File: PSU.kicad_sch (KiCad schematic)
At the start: 11 parts, among them J1 Mini USB Female, J2 Battery Connector, U3 AMS1117-3.3

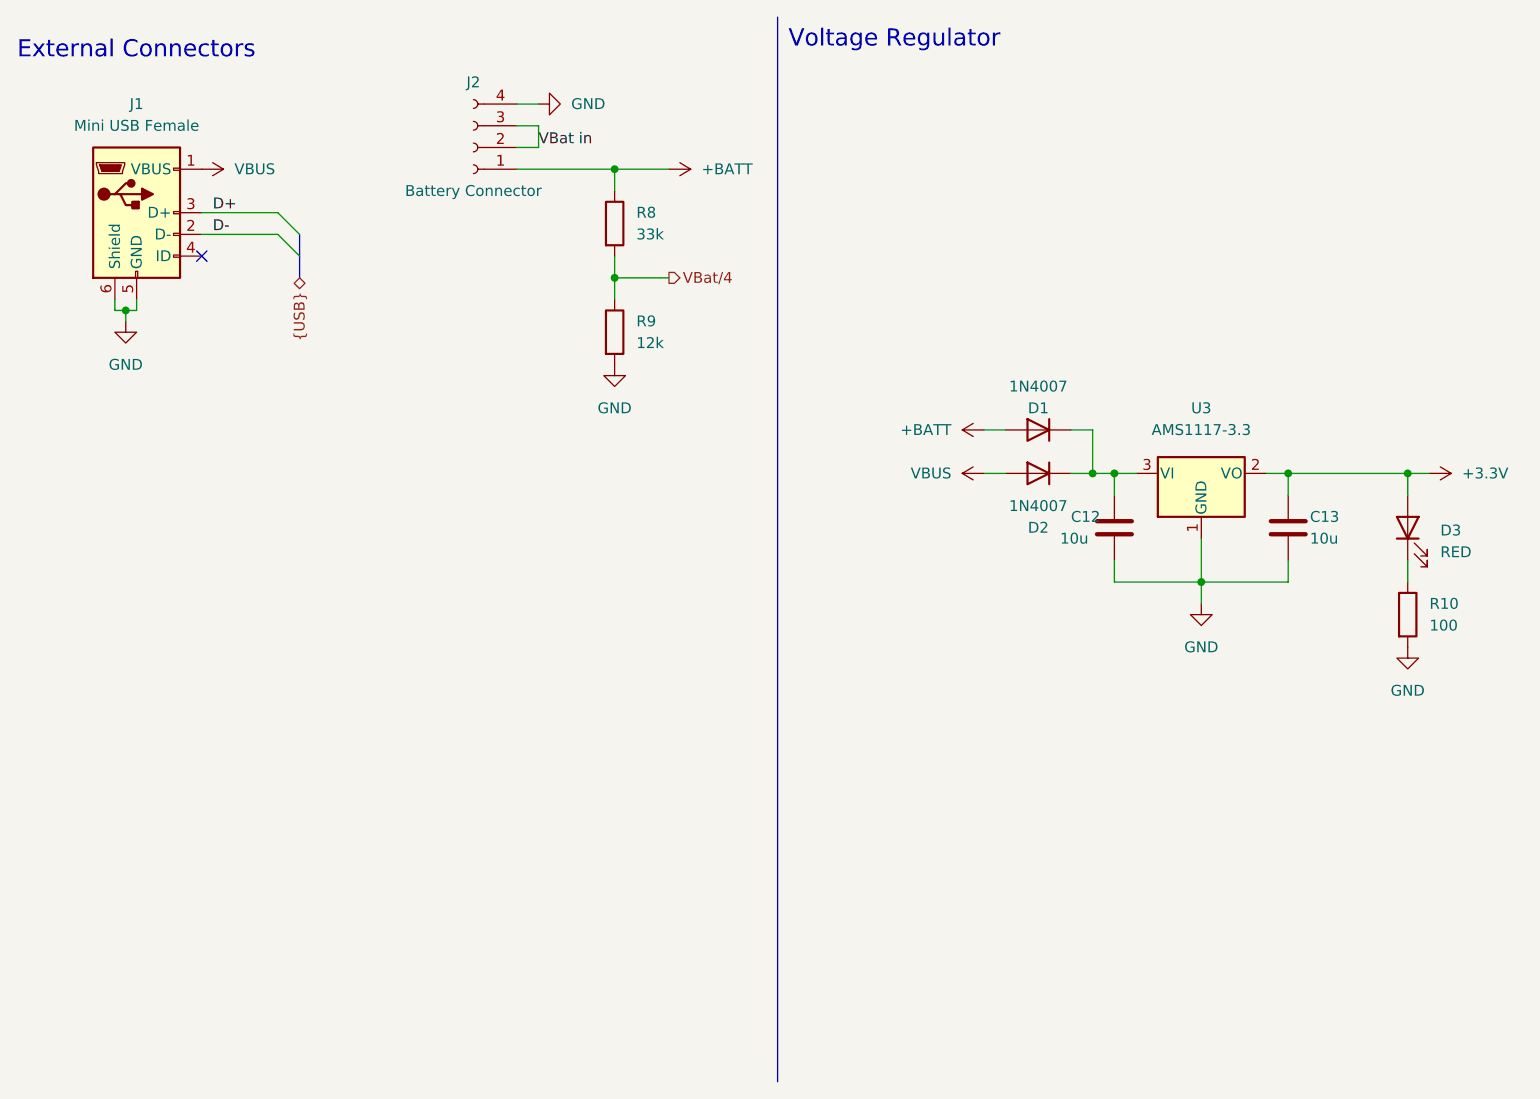
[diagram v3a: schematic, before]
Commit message: Connected the sensors, flash chip, Need to connect the radio and GPS
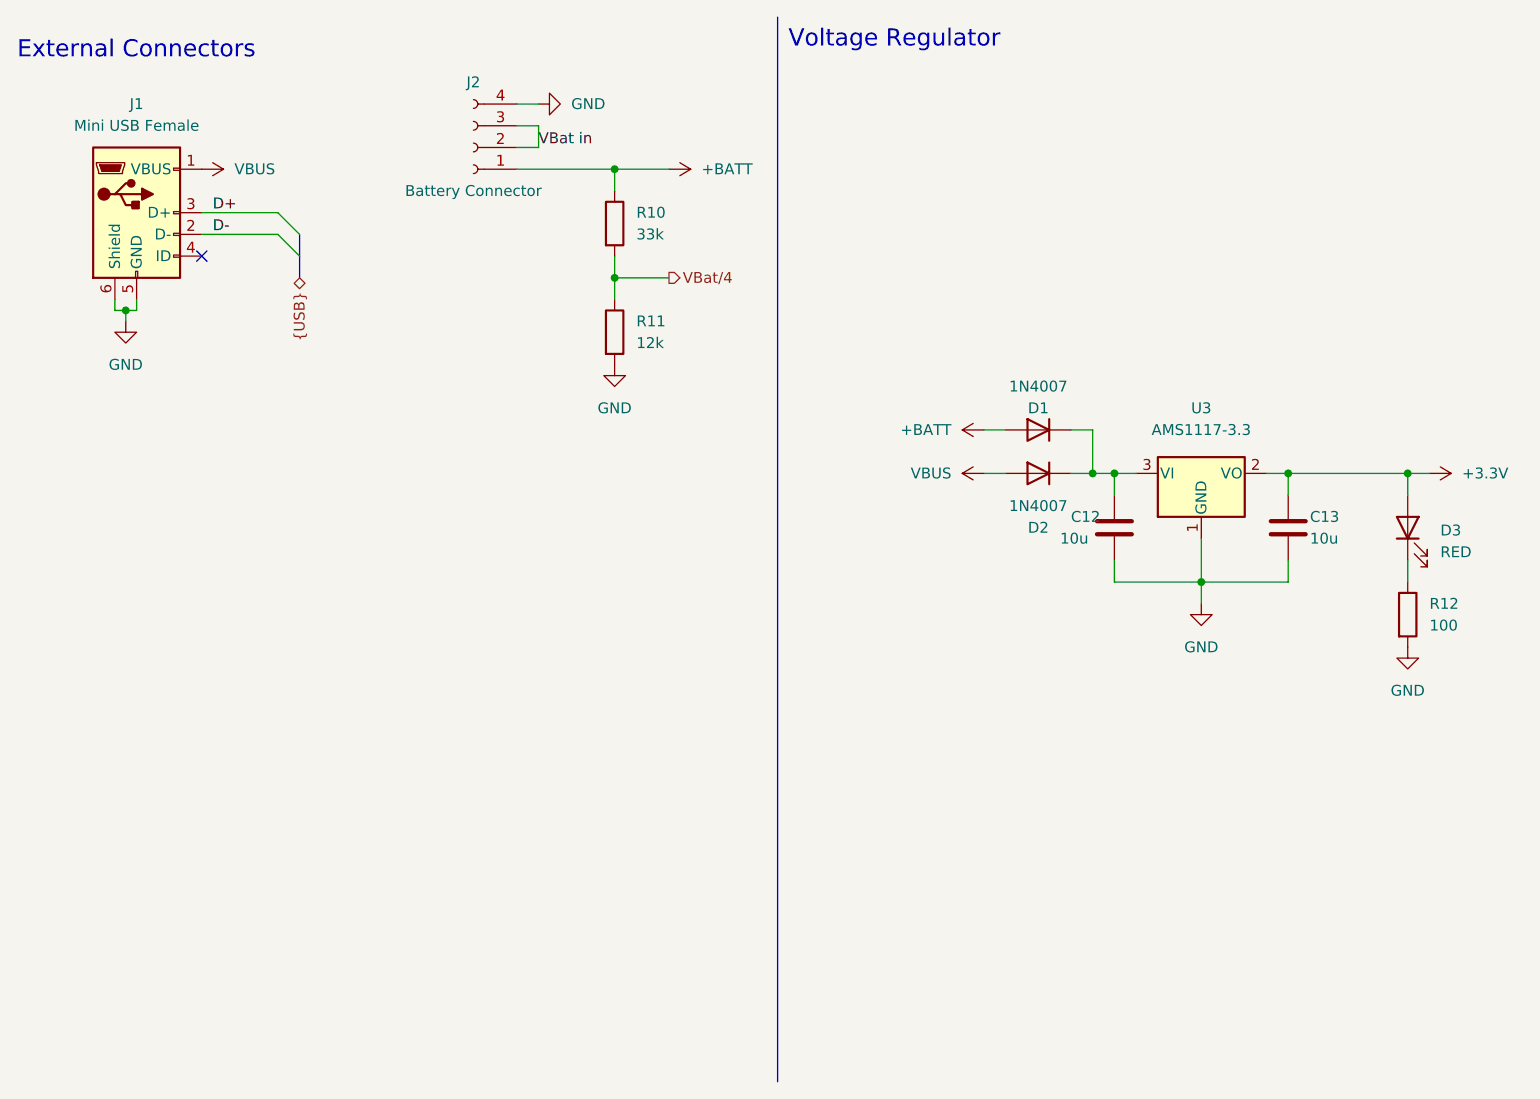
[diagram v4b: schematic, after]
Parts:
- renumbered R8 to R10, R9 to R11, R10 to R12
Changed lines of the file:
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@@
   (symbol (lib_id "power:+3.3V") (at 177.8 64.77 270) (unit 1)
     (in_bom yes) (on_board yes) (fields_autoplaced)
-    (property "Reference" "#PWR026" (id 0) (at 173.99 64.77 0)
+    (property "Reference" "#PWR027" (id 0) (at 173.99 64.77 0)
       (effects (font (size 1.27 1.27)) hide)
     )
@@
   (symbol (lib_id "Device:R") (at 82.55 35.56 0) (unit 1)
     (in_bom yes) (on_board yes) (fields_autoplaced)
-    (property "Reference" "R8" (id 0) (at 85.09 34.2899 0)
+    (property "Reference" "R10" (id 0) (at 85.09 34.2899 0)
       (effects (font (size 1.27 1.27)) (justify left))
     )
@@
   (symbol (lib_id "power:+BATT") (at 88.9 29.21 270) (unit 1)
     (in_bom yes) (on_board yes) (fields_autoplaced)
-    (property "Reference" "#PWR021" (id 0) (at 85.09 29.21 0)
+    (property "Reference" "#PWR022" (id 0) (at 85.09 29.21 0)
       (effects (font (size 1.27 1.27)) hide)
     )
@@
   (symbol (lib_id "power:GND") (at 175.26 85.09 0) (unit 1)
     (in_bom yes) (on_board yes) (fields_autoplaced)
-    (property "Reference" "#PWR025" (id 0) (at 175.26 91.44 0)
+    (property "Reference" "#PWR026" (id 0) (at 175.26 91.44 0)
       (effects (font (size 1.27 1.27)) hide)
     )
@@
   (symbol (lib_id "power:GND") (at 25.4 46.99 0) (unit 1)
     (in_bom yes) (on_board yes) (fields_autoplaced)
-    (property "Reference" "#PWR017" (id 0) (at 25.4 53.34 0)
+    (property "Reference" "#PWR018" (id 0) (at 25.4 53.34 0)
       (effects (font (size 1.27 1.27)) hide)
     )
@@
   (symbol (lib_id "power:VBUS") (at 34.29 29.21 270) (unit 1)
     (in_bom yes) (on_board yes) (fields_autoplaced)
-    (property "Reference" "#PWR018" (id 0) (at 30.48 29.21 0)
+    (property "Reference" "#PWR019" (id 0) (at 30.48 29.21 0)
       (effects (font (size 1.27 1.27)) hide)
     )
@@
   (symbol (lib_id "Device:R") (at 82.55 48.26 0) (unit 1)
     (in_bom yes) (on_board yes) (fields_autoplaced)
-    (property "Reference" "R9" (id 0) (at 85.09 46.9899 0)
+    (property "Reference" "R11" (id 0) (at 85.09 46.9899 0)
       (effects (font (size 1.27 1.27)) (justify left))
     )
@@
   (symbol (lib_id "Device:R") (at 175.26 81.28 0) (unit 1)
     (in_bom yes) (on_board yes) (fields_autoplaced)
-    (property "Reference" "R10" (id 0) (at 177.8 80.0099 0)
+    (property "Reference" "R12" (id 0) (at 177.8 80.0099 0)
       (effects (font (size 1.27 1.27)) (justify left))
     )
@@
   (symbol (lib_id "power:GND") (at 82.55 52.07 0) (unit 1)
     (in_bom yes) (on_board yes) (fields_autoplaced)
-    (property "Reference" "#PWR020" (id 0) (at 82.55 58.42 0)
+    (property "Reference" "#PWR021" (id 0) (at 82.55 58.42 0)
       (effects (font (size 1.27 1.27)) hide)
     )
@@
   (symbol (lib_id "power:VBUS") (at 125.73 64.77 90) (mirror x) (unit 1)
     (in_bom yes) (on_board yes) (fields_autoplaced)
-    (property "Reference" "#PWR023" (id 0) (at 129.54 64.77 0)
+    (property "Reference" "#PWR024" (id 0) (at 129.54 64.77 0)
       (effects (font (size 1.27 1.27)) hide)
     )
@@
   (symbol (lib_id "power:GND") (at 151.13 80.01 0) (unit 1)
     (in_bom yes) (on_board yes) (fields_autoplaced)
-    (property "Reference" "#PWR024" (id 0) (at 151.13 86.36 0)
+    (property "Reference" "#PWR025" (id 0) (at 151.13 86.36 0)
       (effects (font (size 1.27 1.27)) hide)
     )
@@
   (symbol (lib_id "power:GND") (at 73.66 21.59 90) (unit 1)
     (in_bom yes) (on_board yes) (fields_autoplaced)
-    (property "Reference" "#PWR019" (id 0) (at 80.01 21.59 0)
+    (property "Reference" "#PWR020" (id 0) (at 80.01 21.59 0)
       (effects (font (size 1.27 1.27)) hide)
     )
@@
   (symbol (lib_id "power:+BATT") (at 125.73 59.69 90) (mirror x) (unit 1)
     (in_bom yes) (on_board yes) (fields_autoplaced)
-    (property "Reference" "#PWR022" (id 0) (at 129.54 59.69 0)
-      (effects (font (size 1.27 1.27)) hide)
-    )
+    (property "Reference" "#PWR023" (id 0) (at 129.54 59.69 0)
+      (effects (font (size 1.27 1.27)) hide)
+    )

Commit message: Removed GPIO, changed footprints
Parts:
- J2: footprint Connector_Phoenix_MC_HighVoltage:PhoenixContact_MCV_1,5_4-G-5.08_1x04_P5.08mm_Vertical -> YAR_Connectors:ScrewTerm_2.54x04
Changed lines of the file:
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@@
     (property "Reference" "J2" (id 0) (at 66.04 19.05 0))
     (property "Value" "Battery Connector" (id 1) (at 66.04 31.75 0))
-    (property "Footprint" "Connector_Phoenix_MC_HighVoltage:PhoenixContact_MCV_1,5_4-G-5.08_1x04_P5.08mm_Vertical" (id 2) (at 66.04 26.67 0)
+    (property "Footprint" "YAR_Connectors:ScrewTerm_2.54x04" (id 2) (at 66.04 26.67 0)
       (effects (font (size 1.27 1.27)) hide)
     )

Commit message: Rearrange parts of PCB
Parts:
- R10, R11: footprint (none) -> Resistor_SMD:R_0603_1608Metric
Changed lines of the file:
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@@
       (effects (font (size 1.27 1.27)) (justify left))
     )
-    (property "Footprint" "" (id 2) (at 80.772 35.56 90)
+    (property "Footprint" "Resistor_SMD:R_0603_1608Metric" (id 2) (at 80.772 35.56 90)
       (effects (font (size 1.27 1.27)) hide)
     )
@@
       (effects (font (size 1.27 1.27)) (justify left))
     )
-    (property "Footprint" "" (id 2) (at 80.772 48.26 90)
+    (property "Footprint" "Resistor_SMD:R_0603_1608Metric" (id 2) (at 80.772 48.26 90)
       (effects (font (size 1.27 1.27)) hide)
     )
